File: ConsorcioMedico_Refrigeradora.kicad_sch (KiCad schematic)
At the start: 118 parts, among them J1 BatteryHolder, J10 Screw_Terminal_01x01, J11 Screw_Terminal_01x01, J12 Screw_Terminal_01x01, J13 Screw_Terminal_01x01, J14 Screw_Terminal_01x01, J15 Screw_Terminal_01x01, J3 Screw_Terminal_01x01, J37 SWD, J5 Screw_Terminal_01x01, J5 USART, J8 Screw_Terminal_01x01, J9 Screw_Terminal_01x01, K1 HF46F-G/012-HS1T, K2 T9AS1D12-12, K3 HF46F-G/012-HS1T, K4 HF46F-G/012-HS1T, Q1 BSS123, Q1 MMBT3904, Q2 BSS123, Q2 MMBT3904, Q3 MMBT3904, Q4 MMBT3904, U1 STM32F411RETx, U13 INA350, U2 IRM-02, U3 LDL1117

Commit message: SCH: Falta definir los capacitores de entrada, colocar el footprint del diodo e inductor. PCB: Falta acomodar algunos componentes.
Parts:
- removed C44 (x2): 100nF 50V, 1-Capacitor:C_0805_2012Metric, symbol 1-Capacitor:C_0805
- removed C45 (x4): 1uF 50V, 1-Capacitor:C_0603_1608Metric, symbol 1-Capacitor:C_0603
- removed D1, D7, D8: L-144IDT, 1-Led:LED_3.9x1.9mm, symbol 1-Led:LED_Rect
- removed D27 (x2): RED, 1-Led:LED_0805, symbol 1-Led:LED_0805
- removed D7 (x2), D8 (x2): 1N4148WS, Diode_SMD:D_SOD-323, symbol Diode:1N4148WS
- removed D9: LED_0805, 1-Led:LED_0805, symbol 1-Led:LED_0805
- removed J10, J11, J12, J13, J14, J15, J3, J5, J8, J9: Screw_Terminal_01x01, 1-Pad:PAD_D2.60mm_Drill1.4mm, symbol Connector:Screw_Terminal_01x01
- removed J? (x2): Screw_Terminal_01x02, 1-Terminal-Block:DG504-5.08-02P_or_SMKDS 2,5-2-5.08, symbol 1-Terminal-Block:DG504-5.08-02P
- removed K1, K3, K4: HF46F-G/012-HS1T, 1-Relay:Relay_HONGFA_SPST-NO_20.5x7x15.3mm, symbol 1-Relay:Relay_HONGFA_SPST-NO_20.5x7x15.3mm
- removed K2: T9AS1D12-12, 1-Relay:Relay_TE-Connectivity_SPST-NO_32.5x27.4x27.9mm, symbol 1-Relay:Relay_TE_SPST-NO_32.5x27.4x27.9mm
- removed LED1: LFD080AUE-103A-0, 1-Display:LFD080AUE-103A-0, symbol 1-Display:LFD080AUE-103A-0
- removed Q1 (x2), Q2 (x2): BSS123, Package_TO_SOT_SMD:SOT-23, symbol Transistor_FET:BSS123
- removed Q1, Q2, Q3, Q4: MMBT3904, Package_TO_SOT_SMD:SOT-23, symbol Transistor_BJT:MMBT3904
- removed R10, R11, R12, R13, R14, R7, R8, R9: 120R, 1-Resistor:R_0603_1608Metric, symbol 1-Resistor:R_0603
- removed R15 (x2), R17 (x2): 220R, 1-Resistor:R_0805_2012Metric, symbol 1-Resistor:R_0805
- removed R15, R16, R17, R18, R19, R20: 10k, 1-Resistor:R_0603_1608Metric, symbol 1-Resistor:R_0603
- removed R16 (x2), R18 (x2): 10K, 1-Resistor:R_0805_2012Metric, symbol 1-Resistor:R_0805
- removed R167 (x2): 3.9k, 1-Resistor:R_0805_2012Metric, symbol 1-Resistor:R_0805
- removed R169 (x4): 1k, 1-Resistor:R_0805_2012Metric, symbol 1-Resistor:R_0805
- removed R176 (x2): 2.7k, 1-Resistor:R_0805_2012Metric, symbol 1-Resistor:R_0805
- removed R2, R209 (x2), R4, R5, R6: 1k, 1-Resistor:R_0603_1608Metric, symbol 1-Resistor:R_0603
- removed R6 (x3): 330, 1-Resistor:R_0603_1608Metric, symbol 1-Resistor:R_0603
- removed R6: 1000, 1-Resistor:R_0603_1608Metric, symbol 1-Resistor:R_0603
- removed S1: Buzz, 1-Switch:SW_PUSH-12mm-H, symbol 1-Switch:SW_PUSH_12mm_H
- removed S2: Touch, 1-Switch:SW_PUSH-12mm-H, symbol 1-Switch:SW_PUSH_12mm_H
- removed S3: Up, 1-Switch:SW_PUSH-12mm-H, symbol 1-Switch:SW_PUSH_12mm_H
- removed S4: Down, 1-Switch:SW_PUSH-12mm-H, symbol 1-Switch:SW_PUSH_12mm_H
- removed S5: Cooling, 1-Switch:SW_PUSH-12mm-H, symbol 1-Switch:SW_PUSH_12mm_H
- removed S6: Light, 1-Switch:SW_PUSH-12mm-H, symbol 1-Switch:SW_PUSH_12mm_H
- removed U13 (x2): INA350, 1-Package_TO_SOT_SMD:SOT-23-8, symbol 1-IC-Amplifier:INA350_SOT-23-8
- added C29: 470uF, 1-Capacitor:C_1206_3216Metric, symbol 1-Capacitor:C_1206
- added C31, C32: 1uF, 1-Capacitor:C_0805_2012Metric, symbol 1-Capacitor:C_0805
- added C33: 180uF, 1-Capacitor:C_1206_3216Metric, symbol 1-Capacitor:C_1206
- added D2: MBRS140T3G, symbol Device:D_Schottky
- added J5: USART, 1-Pinhead:PinHeader_1x04_P2.54mm_Vertical, symbol Connector:Screw_Terminal_01x04
- added J?: Screw_Terminal_01x02, 1-Terminal-Block:DG504-5.08-02P_or_SMKDS 2,5-2-5.08, symbol 1-Terminal-Block:DG504-5.08-02P
- added L1: FNR6045S680MT, symbol Device:L
- added R24, R29: 2.2k, 1-Resistor:R_0603_1608Metric, symbol 1-Resistor:R_0603
- added U8: LM2594HVM-5.0, Package_SO:SOIC-8_3.9x4.9mm_P1.27mm, symbol Regulator_Switching:LM2594HVM-5.0
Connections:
- net MCU_RX6 is gone; now on net MCU_RX1: J5.2 (Pin_2)
- net MCU_TX6 is gone; now on net MCU_TX1: J5.3 (Pin_3)
- net +3.3V: now also J5.1 (Pin_1), R24.2, R29.2
- net +5V: now also C32.1, C33.2, L1.2, U8.4 (FB); no longer C13.1, U2.+V (+)
- net Button_Buzzer: now also U1.56 (PB4); no longer U1.55 (PB3)
- net Button_Cooling: now also U1.61 (PB8); no longer U1.59 (PB7)
- net Button_Down: now also U1.59 (PB7); no longer U1.58 (PB6)
- net Button_Light: now also U1.62 (PB9); no longer U1.61 (PB8)
- net Button_Touch: now also U1.57 (PB5); no longer U1.56 (PB4)
- net Button_Up: now also U1.58 (PB6); no longer U1.57 (PB5)
- net GND: now also C29.1, C31.2, C32.2, C33.1, D2.2 (A), J5.4 (Pin_4)
- net LED_Defrost: now also U1.34 (PB13); no longer U1.46 (PA13)
- net LED_Door: now also U1.35 (PB14); no longer U1.49 (PA14)
- net LED_Status: now also U1.33 (PB12); no longer U1.45 (PA12)
- net LED_TempAlarm: now also U1.36 (PB15); no longer U1.50 (PA15)
- net RTD1: now also U1.24 (PC4)
- net RTD2: now also U1.25 (PC5)
- net Relay_Calefac: now also U1.2 (PC13); no longer U1.38 (PC7)
- net Relay_Compressor: now also U1.53 (PC12); no longer U1.37 (PC6)
- net Relay_Fan: now also U1.51 (PC10); no longer U1.24 (PC4)
- net Relay_Light: now also U1.52 (PC11); no longer U1.25 (PC5)
- net SWCLK: now also U1.49 (PA14)
- net SWDIO: now also U1.46 (PA13)
- net SWO: now also U1.55 (PB3)
- net at U2.AC1: now also J?.1 (Pin_1)
- net at U2.AC2: now also J?.2 (Pin_2)
- net DIG_IN_0: now reaches U1.39 (PC8)
- net I2C3_SDA: now reaches U1.40 (PC9)
- net I2C3_SDA: now also J5.2 (Pin_2), R29.1
- net I2C3_SCL: now reaches U1.41 (PA8)
- net I2C3_SCL: now also J5.3 (Pin_3), R24.1
- net MCU_TX1: now reaches U1.42 (PA9)
- net MCU_RX1: now reaches U1.43 (PA10)
- net USB_DM: now reaches U1.44 (PA11)
- new net: D2.1 (K), L1.1, U8.8 (OUT)
- new net +12V: C13.1, C29.2, C31.1, U2.+V (+), U8.7 (VIN)
- new net DIG_IN_1: U1.38 (PC7)
- new net USB_DP: U1.45 (PA12)
- no-connect marks 4 -> 9
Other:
- added sheet Analog (Analog.kicad_sch)
- added sheet Dig_Inputs (Dig_Inputs.kicad_sch)
- added sheet Dig_Outputs (Dig_Outputs.kicad_sch)
- added sheet Relay (Relay.kicad_sch)
- note added: "ADC"
- note added: "BUTTON"
- note added: "C13585"
- note added: "C28323"
- note added: "DISLAY"
- note added: "I2C3"
- note added: "INPUTS"
- note added: "LED"
- note added: "Microcontroller: STM32F411RET6: C94355 Crystal 8Mhz: C115962 Driver Display: C256866 BSS806:C91714 2k 0805: C17604 VoltageSupply 12v->5v LM2594: C2904795 MBRS140T3G:C5377815 FNR6045S680MT:C168091 220uF 50V: C125977"
- note added: "RELAY"
- note added: "SWD"
- note added: "USART1"
- note added: "USB"
- note removed: "0.05V"
- note removed: "1V"
- note removed: "ANALOG"
- note removed: "BUTTONS"
- note removed: "Fuente de voltaje"
- note removed: "LEDS"
- note removed: "Potencia: 12V 720R = 16mA 12V 144R = 83mA 3x16 + 83 = 131mA -> Potencia regulador: 12V*131mA = 1.57W"
- note removed: "RTD: PT100 I = 500uA"
- note removed: "Relay Compressor + Condensador"
- note removed: "Relay Luz"
- note removed: "Relay Resistencia"
- note removed: "Relay Ventilador del Evaporador"
- note removed: "STM32F411RET6: C94355 Crystal 8Mhz: C115962"
- moved on the sheet: C13, C8, C9, C?, J1, J37, J5, R?, U1, U2, U3, Y?

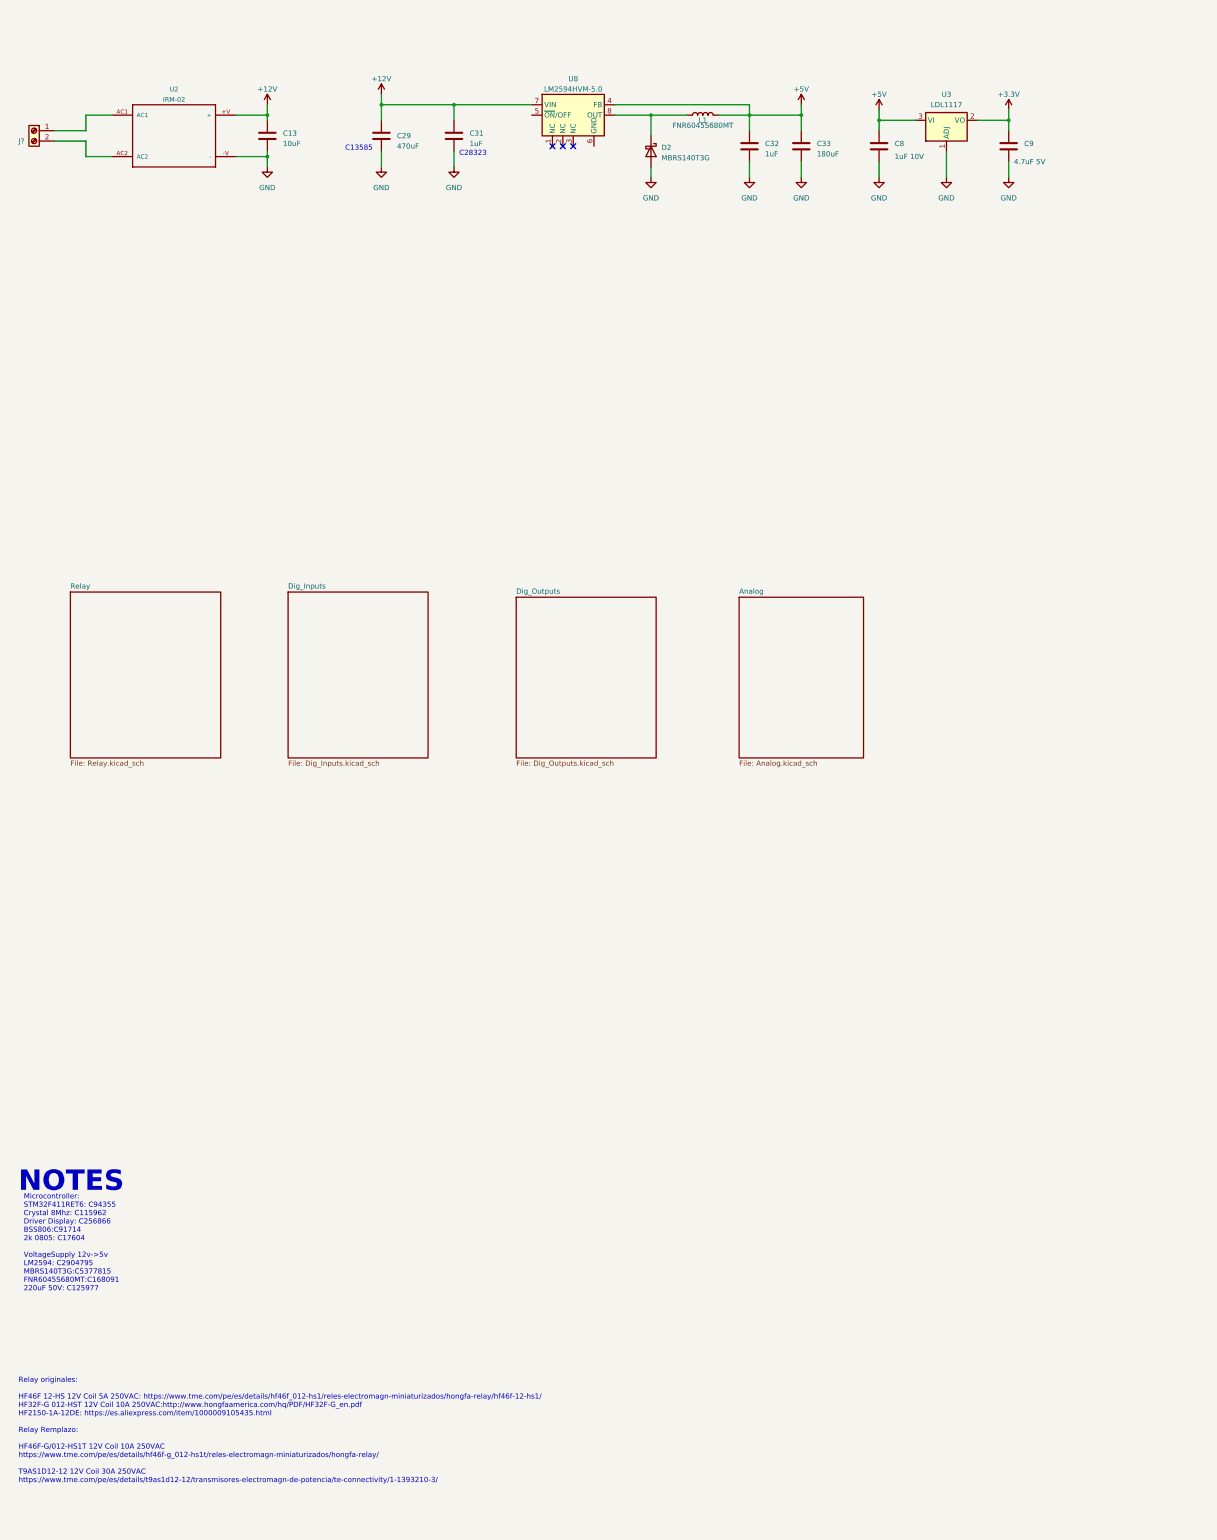
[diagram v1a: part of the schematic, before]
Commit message: SCH: Se cambió el IRM, se colocó filtro en la entrada AC, se modificó la fuente switching LM, se corrigieron algunos errores de diseño. PCB: Se terminó el placement de los componentes
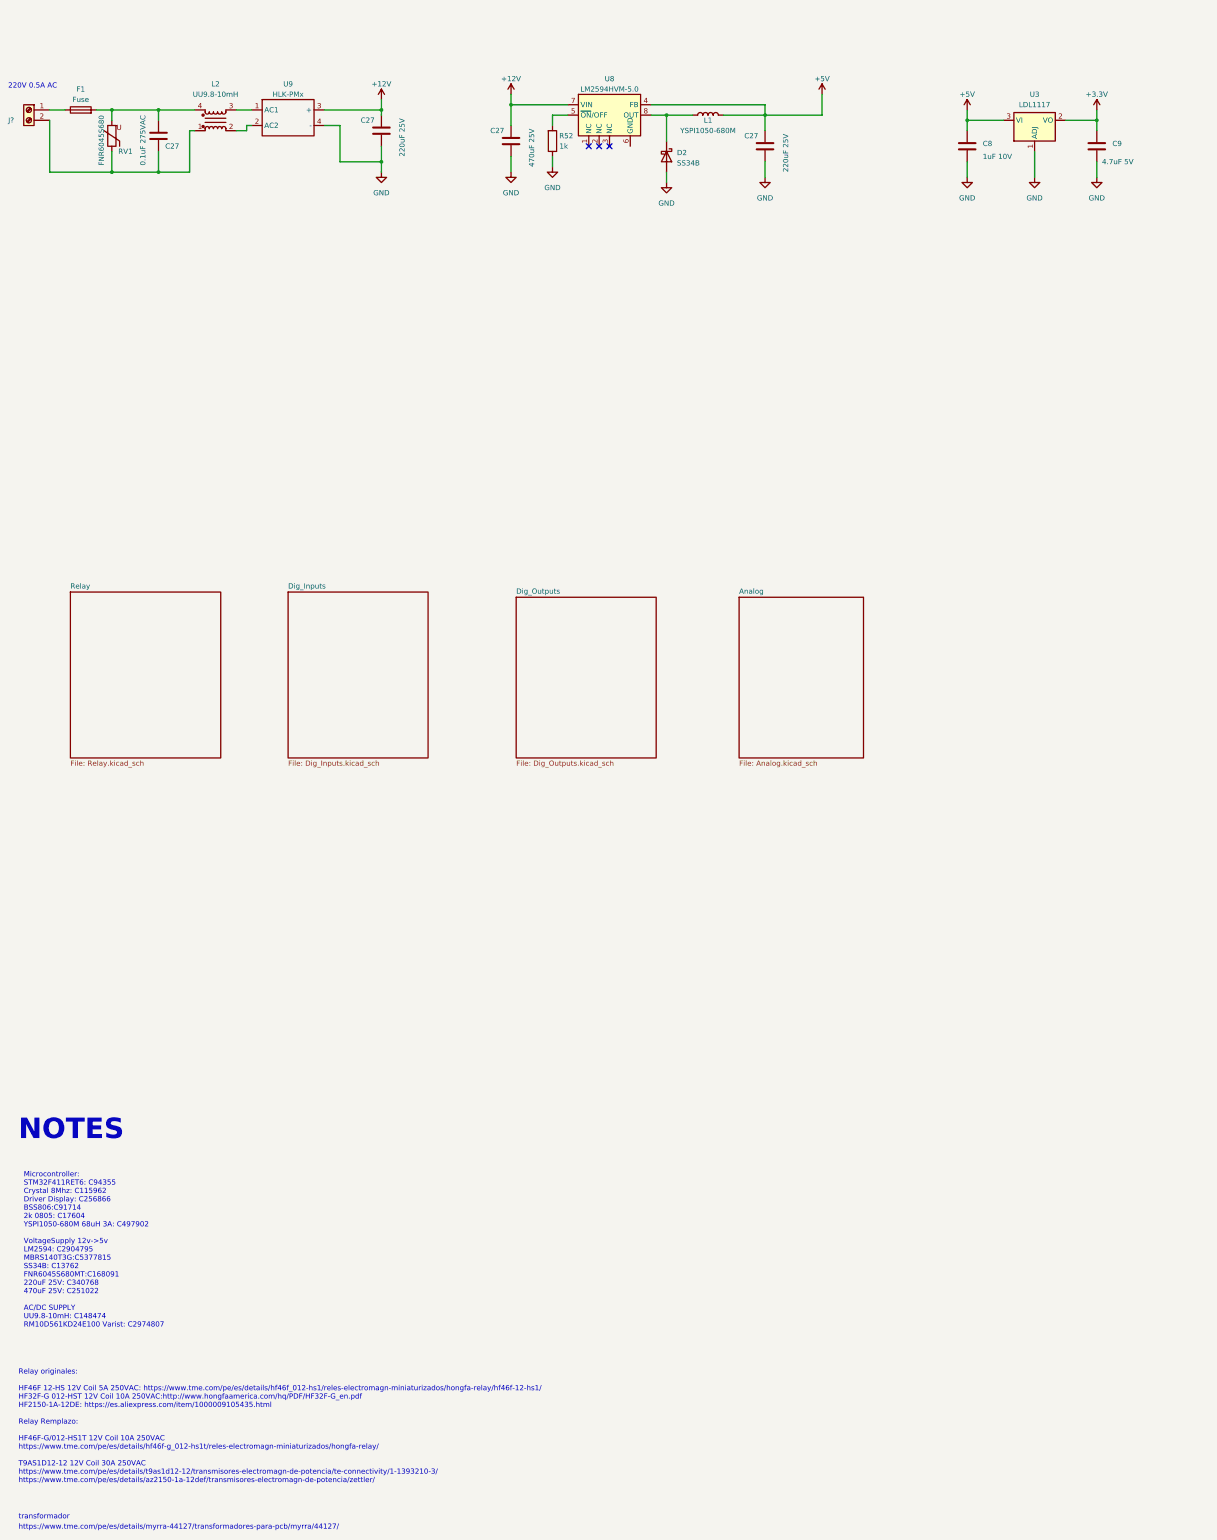
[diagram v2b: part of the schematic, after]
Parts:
- removed C13: 10uF, 1-Capacitor:C_1206_3216Metric, symbol 1-Capacitor:C_1206
- removed C29: 470uF, 1-Capacitor:C_1206_3216Metric, symbol 1-Capacitor:C_1206
- removed C31, C32: 1uF, 1-Capacitor:C_0805_2012Metric, symbol 1-Capacitor:C_0805
- removed C33: 180uF, 1-Capacitor:C_1206_3216Metric, symbol 1-Capacitor:C_1206
- removed U2: IRM-02, 1-Supply_Module-Eagle:IRM-02, symbol 1-Supply_Module-Eagle:IRM-02
- added C27: 0.1uF 275VAC, Capacitor_THT:C_Rect_L18.0mm_W5.0mm_P15.00mm_FKS3_FKP3, symbol Device:C
- added C27: 470uF 25V, Capacitor_SMD:CP_Elec_10x10, symbol Device:C
- added C27 (x2): 220uF 25V, Capacitor_SMD:CP_Elec_6.3x7.7, symbol Device:C
- added F1: Fuse, Fuse:Fuseholder_TR5_Littelfuse_No560_No460, symbol Device:Fuse
- added L2: UU9.8-10mH, 1-Inductor:UU9.8-10mH, symbol 1-Inductor:UU9.8-10mH
- added R52: 1k, 1-Resistor:R_0603_1608Metric, symbol 1-Resistor:R_0603
- added RV1: FNR6045S680, Varistor:RV_Disc_D12mm_W5.1mm_P7.5mm, symbol Device:Varistor
- added U9: HLK-PMx, 1-Module:HLK-PM12, symbol 1-Module:HLK-PM-03/01/09/12
- D2: value MBRS140T3G -> SS34B; footprint (none) -> 1-Diode:D_SMB
- L1: value FNR6045S680MT -> YSPI1050-680M; footprint (none) -> Inductor_SMD:L_10.4x10.4_H4.8
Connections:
- net +12V: now also C27.1, C27.1, U9.3 (+)
- net +5V: now also C27.1
- net GND: now also C27.2, C27.2, C27.2, R52.1, U9.4 (-)
- net at J?.1 (Pin_1): now also F1.1
- net at J?.2 (Pin_2): now also C27.1, L2.1, RV1.1
- net at U8.5 (~{ON}/OFF): now also R52.2
- new net: C27.2, F1.2, L2.4, RV1.2
- new net: L2.3, U9.1 (AC1)
- new net: L2.2, U9.2 (AC2)
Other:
- note added: "220V 0.5A AC"
- note added: "Microcontroller: STM32F411RET6: C94355 Crystal 8Mhz: C115962 Driver Display: C256866 BSS806:C91714 2k 0805: C17604 YSPI1050-680M 68uH 3A: C497902 VoltageSupply 12v->5v LM2594: C2904795 MBRS140T3G:C5377815 SS34B: C13762 FNR6045S680MT:C168091 220uF 25V: C340768 470uF 25V: C251022 AC/DC SUPPLY UU9.8-10mH: C148474 RM10D561KD24E100 Varist: C2974807"
- note added: "https://www.tme.com/pe/es/details/myrra-44127/transformadores-para-pcb/myrra/44127/"
- note added: "transformador"
- note removed: "C13585"
- note removed: "C28323"
- note removed: "Microcontroller: STM32F411RET6: C94355 Crystal 8Mhz: C115962 Driver Display: C256866 BSS806:C91714 2k 0805: C17604 VoltageSupply 12v->5v LM2594: C2904795 MBRS140T3G:C5377815 FNR6045S680MT:C168091 220uF 50V: C125977"
- moved on the sheet: C8, C9, D2, J?, L1, U3, U8

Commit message: Se guarda avance
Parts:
- C27: value 470uF 25V -> 68uF 25V; footprint Capacitor_SMD:CP_Elec_10x10 -> Capacitor_SMD:CP_Elec_6.3x5.7
- C27: value 220uF 25V -> 100uF 25V
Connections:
- net at F1.2, L2.4: now also C27.1, RV1.1; no longer C27.2, RV1.2
- net at J?.2 (Pin_2), L2.1: now also C27.2, RV1.2; no longer C27.1, RV1.1
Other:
- note added: "Microcontroller: STM32F411RET6: C94355 Crystal 8Mhz: C115962 Driver Display: C256866 BSS806:C91714 2k 0805: C17604 YSPI1050-680M 68uH 3A: C497902 VoltageSupply 12v->5v LM2594: C2904795 MBRS140T3G:C5377815 SS34B: C13762 FNR6045S680MT:C168091 220uF 25V: C340768 470uF 25V: C251022 68uH 25V: C249947 AC/DC SUPPLY UU9.8-10mH: C148474 RM10D561KD24E100 Varist: C2974807"
- note removed: "Microcontroller: STM32F411RET6: C94355 Crystal 8Mhz: C115962 Driver Display: C256866 BSS806:C91714 2k 0805: C17604 YSPI1050-680M 68uH 3A: C497902 VoltageSupply 12v->5v LM2594: C2904795 MBRS140T3G:C5377815 SS34B: C13762 FNR6045S680MT:C168091 220uF 25V: C340768 470uF 25V: C251022 AC/DC SUPPLY UU9.8-10mH: C148474 RM10D561KD24E100 Varist: C2974807"
- moved on the sheet: C27, L1, RV1, Y?
